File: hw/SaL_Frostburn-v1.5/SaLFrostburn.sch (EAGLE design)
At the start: 100 parts, among them U1 ATSAMD21G-A, U2 CC1120, U3 ADXL345, U4 gps, Y1 32.768kHx, Y3 32MHz

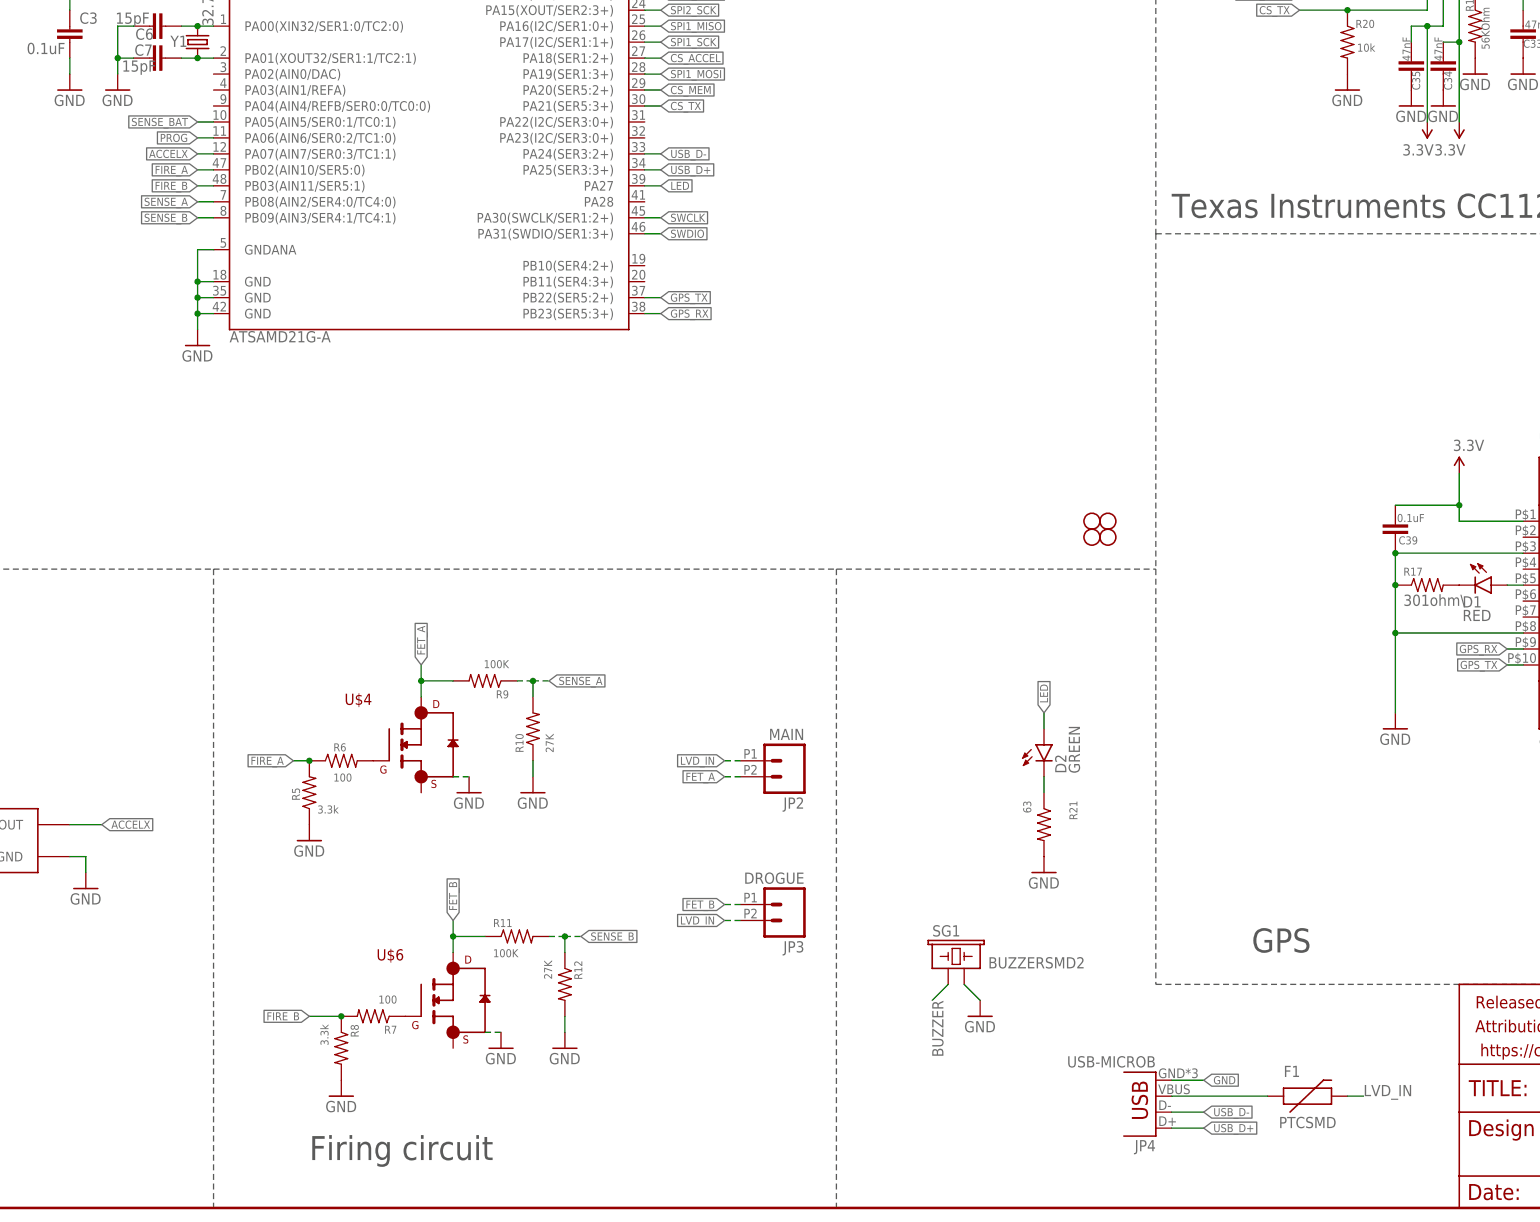
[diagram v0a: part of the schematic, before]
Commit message: SaLFrostburn-v1.1 hw finished and ordered
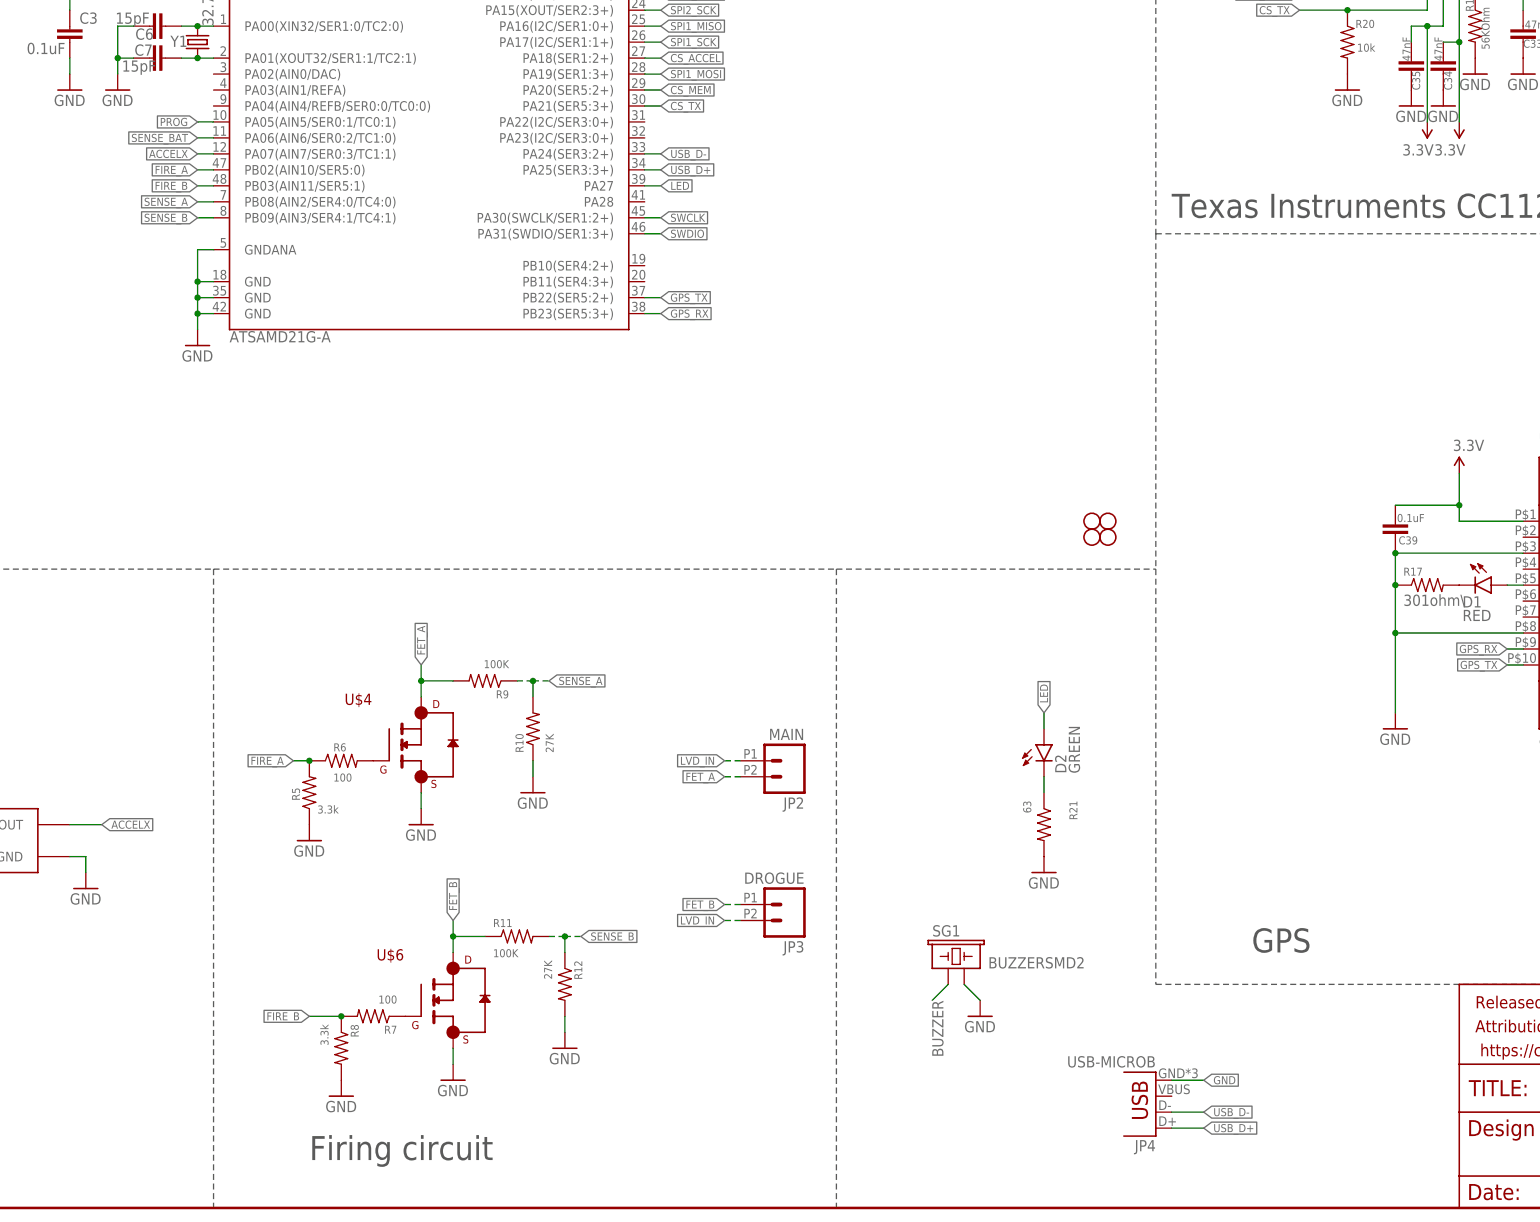
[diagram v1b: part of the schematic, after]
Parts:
- removed F1: PTCSMD, SparkFun-PowerIC:PTCSMD
- renumbered U2 to TX/RX
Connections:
- removed net N$14: F1.1, JP4.VBUS
- net GND: now also U$4.S, U$6.S
- net LVD_IN: no longer F1.2
- net PROG: now also U1.PA05(AIN5/SER0:1/TC0:1); no longer U1.PA06(AIN6/SER0:2/TC1:0)
- net SENSE_BAT: now also U1.PA06(AIN6/SER0:2/TC1:0); no longer U1.PA05(AIN5/SER0:1/TC0:1)

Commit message: small changes to usb drivers
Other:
- note added: "Stephen Arwine"
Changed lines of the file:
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@@
 <wire x1="231.14" y1="101.6" x2="281.94" y2="101.6" width="0.1524" layer="97" style="longdash"/>
 <wire x1="132.08" y1="101.6" x2="132.08" y2="0" width="0.1524" layer="97" style="longdash"/>
+<text x="350.52" y="7.62" size="5.08" layer="97">Stephen Arwine</text>
 </plain>
 <instances>
